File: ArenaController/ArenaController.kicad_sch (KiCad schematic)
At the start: 29 parts, among them J1 RJ45, J2 RJ45, J4 RJ45, J5 RJ45, J6 RJ45, J8 Screw_Terminal_01x04, J9 Barrel_Jack_MountingPin, Q1 FS3400, Q2 FS3400, Q3 FS3400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

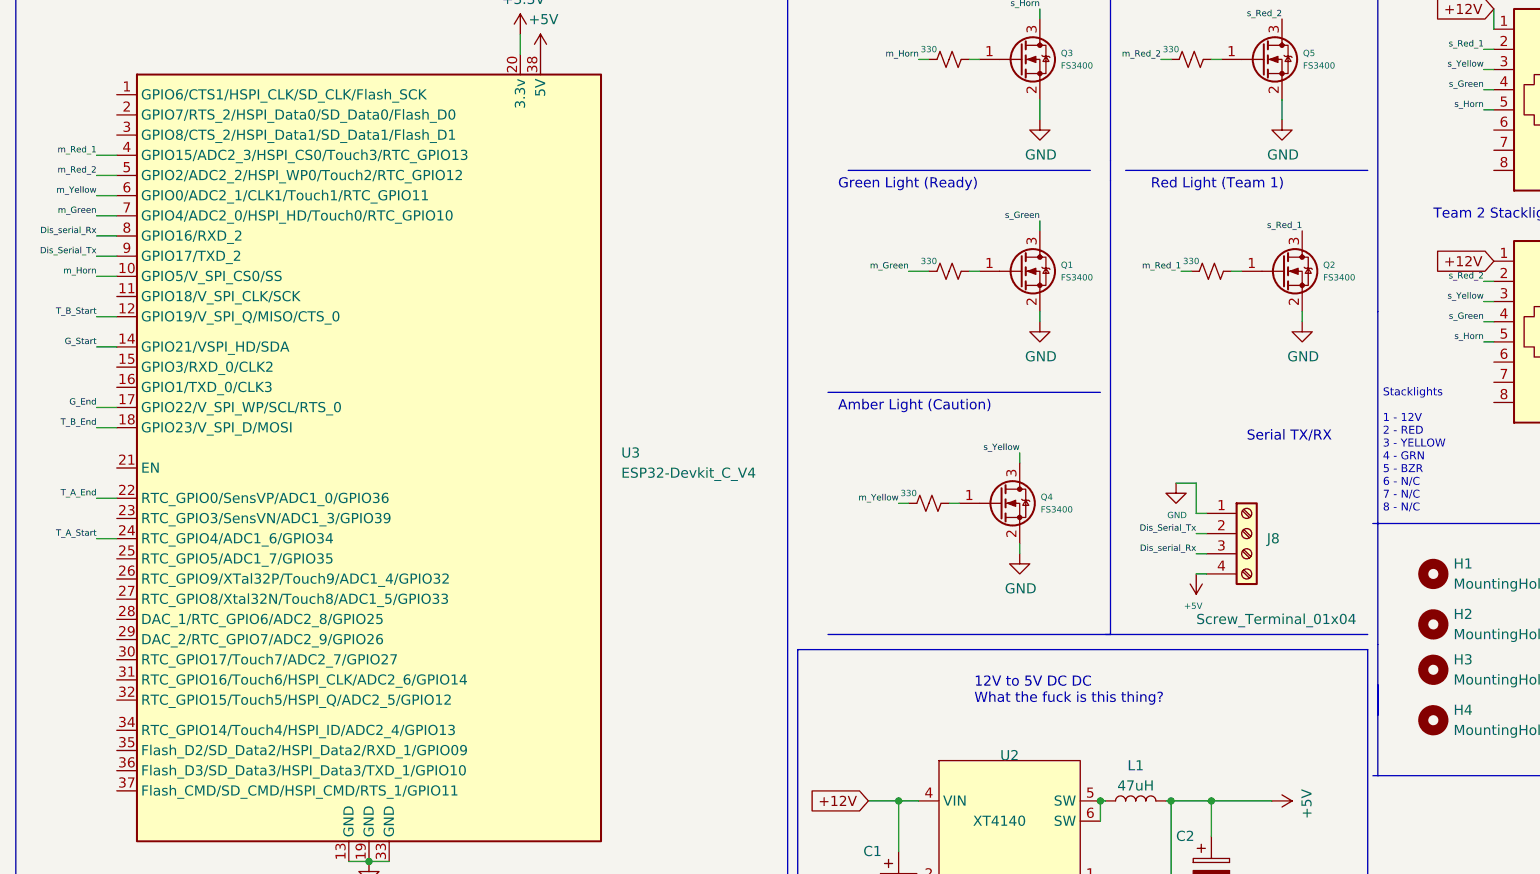
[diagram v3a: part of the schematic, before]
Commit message: Update PCB errors and also remove software from this repo.
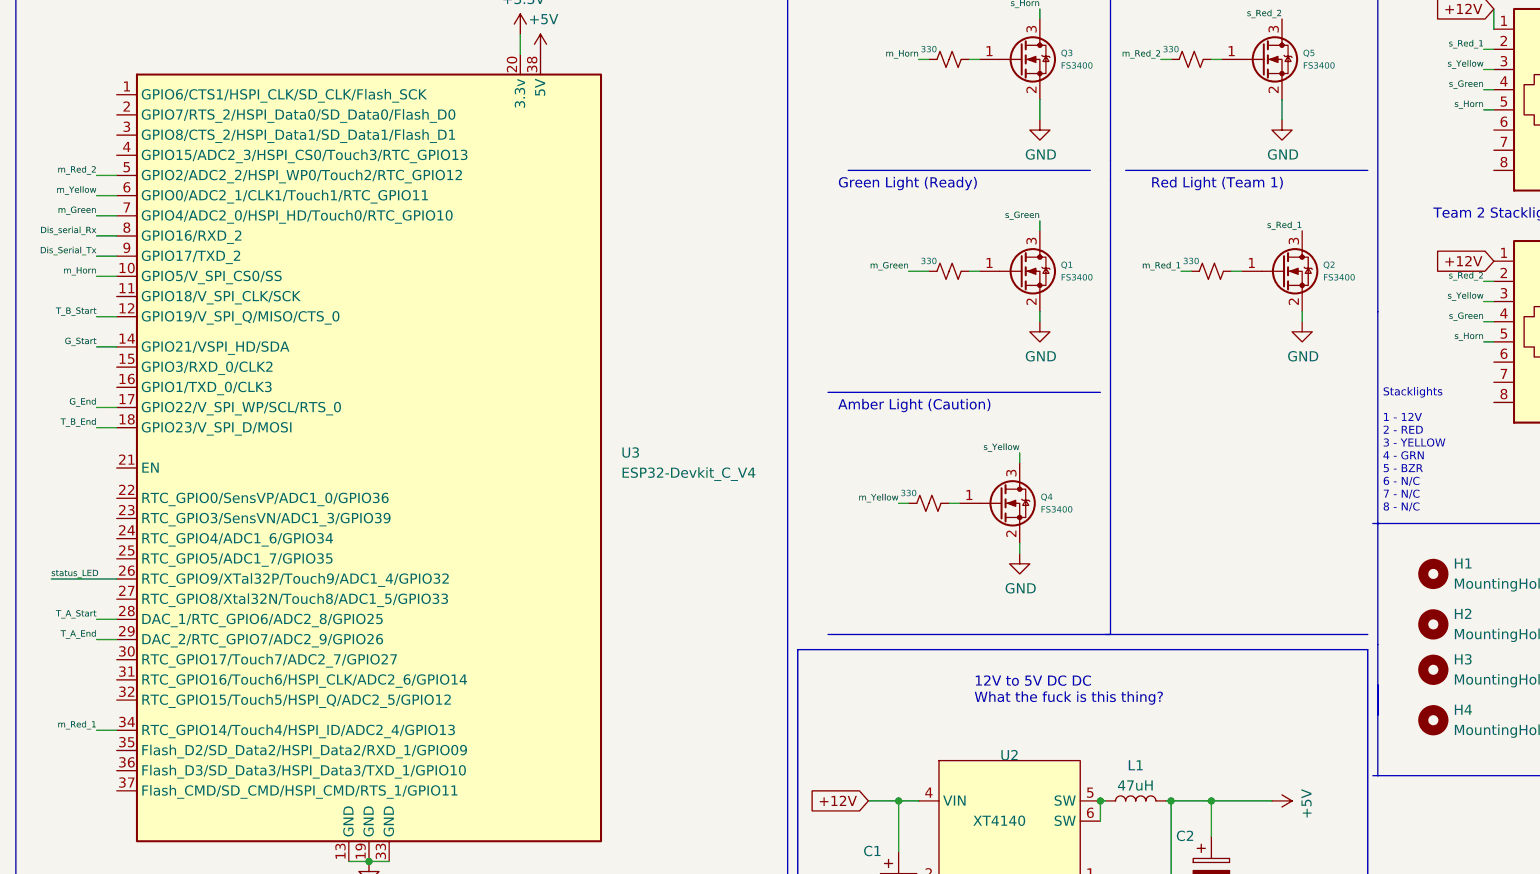
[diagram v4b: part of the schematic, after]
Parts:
- removed J8: Screw_Terminal_01x04, Connector_PinSocket_2.54mm:PinSocket_1x04_P2.54mm_Vertical, symbol Connector:Screw_Terminal_01x04
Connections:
- net T_A_End: now also U3.29 (DAC_2/RTC_GPIO7/ADC2_9/GPIO26); no longer U3.22 (RTC_GPIO0/SensVP/ADC1_0/GPIO36)
- net T_A_Start: now also U3.28 (DAC_1/RTC_GPIO6/ADC2_8/GPIO25); no longer U3.24 (RTC_GPIO4/ADC1_6/GPIO34)
- net m_Red_1: now also U3.34 (RTC_GPIO14/Touch4/HSPI_ID/ADC2_4/GPIO13); no longer U3.4 (GPIO15/ADC2_3/HSPI_CS0/Touch3/RTC_GPIO13)
- net status_LED: now also U3.26 (RTC_GPIO9/XTal32P/Touch9/ADC1_4/GPIO32)
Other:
- note removed: "Serial TX/RX"
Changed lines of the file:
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@@
   (title_block
     (title "Combat Arena Timing Control")
-    (date "2023-04-14")
-    (rev "0.4a")
+    (date "2023-04-29")
+    (rev "0.5")
     (company "Fair Use Building & Research Labs, 501c3")
     (comment 2 "Neil Flynn")
@@
     (stroke (width 0) (type default))
   )
-  (wire (pts (xy 165.735 92.71) (xy 164.465 92.71))
-    (stroke (width 0) (type default))
-  )
   (wire (pts (xy 243.84 63.5) (xy 248.92 63.5))
     (stroke (width 0) (type default))
@@
     (stroke (width 0) (type default))
   )
-  (wire (pts (xy 164.465 83.82) (xy 164.465 87.63))
-    (stroke (width 0) (type default))
-  )
-  (wire (pts (xy 165.735 90.17) (xy 164.465 90.17))
-    (stroke (width 0) (type default))
-  )
   (wire (pts (xy 137.16 30.48) (xy 135.89 30.48))
     (stroke (width 0) (type default))
@@
     (stroke (width 0) (type default))
   )
+  (wire (pts (xy 20.32 95.885) (xy 28.575 95.885))
+    (stroke (width 0) (type default))
+  )
   (polyline (pts (xy 187.325 120.65) (xy 187.325 104.14))
     (stroke (width 0) (type default))
@@
     (stroke (width 0) (type default))
   )
-  (wire (pts (xy 161.925 83.82) (xy 164.465 83.82))
-    (stroke (width 0) (type default))
-  )
   (polyline (pts (xy 227.33 15.24) (xy 227.33 67.31))
     (stroke (width 0) (type default))
@@
     (stroke (width 0) (type default))
   )
-  (wire (pts (xy 28.575 90.805) (xy 26.035 90.805))
+  (wire (pts (xy 28.575 100.965) (xy 26.035 100.965))
     (stroke (width 0) (type default))
   )
@@
     (stroke (width 0) (type default))
   )
-  (wire (pts (xy 165.735 95.25) (xy 164.465 95.25))
-    (stroke (width 0) (type default))
-  )
   (polyline (pts (xy 275.59 48.26) (xy 227.33 48.26))
     (stroke (width 0) (type default))
@@
     (stroke (width 0) (type default))
   )
-  (wire (pts (xy 165.735 87.63) (xy 164.465 87.63))
-    (stroke (width 0) (type default))
-  )
   (wire (pts (xy 57.785 131.445) (xy 60.325 131.445))
     (stroke (width 0) (type default))
@@
     (stroke (width 0) (type default))
   )
-  (wire (pts (xy 28.575 42.545) (xy 26.035 42.545))
+  (wire (pts (xy 28.575 114.935) (xy 26.035 114.935))
     (stroke (width 0) (type default))
   )
@@
     (stroke (width 0) (type default))
   )
-  (wire (pts (xy 28.575 85.725) (xy 26.035 85.725))
+  (wire (pts (xy 28.575 103.505) (xy 26.035 103.505))
     (stroke (width 0) (type default))
   )
@@
     (effects (font (size 1.27 1.27)) (justify left bottom))
   )
-  (text "Serial TX/RX\n" (at 170.815 78.74 0)
-    (effects (font (size 1.27 1.27)) (justify left bottom))
-  )
   (text "Team 1 Stacklight" (at 198.12 19.05 0)
     (effects (font (size 1.27 1.27)) (justify left bottom))
@@
     (effects (font (size 1 1)) (justify left bottom))
   )
-  (label "T_A_End" (at 26.035 85.725 180) (fields_autoplaced)
+  (label "T_A_End" (at 26.035 103.505 180) (fields_autoplaced)
     (effects (font (size 0.7874 0.7874)) (justify right bottom))
   )
@@
     (effects (font (size 0.7874 0.7874)) (justify right bottom))
   )
-  (label "Dis_serial_Rx" (at 164.465 92.71 180) (fields_autoplaced)
-    (effects (font (size 0.7874 0.7874)) (justify right bottom))
-  )
   (label "s_Green" (at 200.66 63.5 180) (fields_autoplaced)
     (effects (font (size 0.7874 0.7874)) (justify right bottom))
@@
     (effects (font (size 0.7874 0.7874)) (justify right bottom))
   )
-  (label "T_A_Start" (at 26.035 90.805 180) (fields_autoplaced)
+  (label "T_A_Start" (at 26.035 100.965 180) (fields_autoplaced)
     (effects (font (size 0.7874 0.7874)) (justify right bottom))
   )
@@
     (effects (font (size 0.7874 0.7874)) (justify right bottom))
   )
-  (label "m_Red_1" (at 26.035 42.545 180) (fields_autoplaced)
+  (label "m_Red_1" (at 26.035 114.935 180) (fields_autoplaced)
     (effects (font (size 0.7874 0.7874)) (justify right bottom))
   )
@@
     (effects (font (size 0.7874 0.7874)) (justify right bottom))
   )
-  (label "Dis_Serial_Tx" (at 164.465 90.17 180) (fields_autoplaced)
-    (effects (font (size 0.7874 0.7874)) (justify right bottom))
+  (label "status_LED" (at 20.32 95.885 0) (fields_autoplaced)
+    (effects (font (size 0.7874 0.7874)) (justify left bottom))
   )
   (label "m_Red_2" (at 160.02 30.48 180) (fields_autoplaced)
@@
     )
   )
-  (symbol (lib_id "power:+5V") (at 164.465 95.25 180) (unit 1)
-    (in_bom yes) (on_board yes) (dnp no)
-    (property "Reference" "#PWR0125" (at 164.465 91.44 0)
-      (effects (font (size 0.7874 0.7874)) hide)
-    )
-    (property "Value" "+5V" (at 164.084 99.2886 0)
-      (effects (font (size 0.7874 0.7874)))
-    )
-    (property "Footprint" "" (at 164.465 95.25 0)
-      (effects (font (size 1.27 1.27)) hide)
-    )
-    (property "Datasheet" "" (at 164.465 95.25 0)
-      (effects (font (size 1.27 1.27)) hide)
-    )
-    (pin "1")
-    (instances
-      (project "ArenaController"
-        (path "/156576da-4c7a-4c71-af43-7540e3a24bd3"
-          (reference "#PWR0125") (unit 1)
-        )
-      )
-    )
-  )
   (symbol (lib_id "symbols:FS3400") (at 175.26 57.15 0) (unit 1)
     (in_bom yes) (on_board yes) (dnp no)
@@
         (path "/156576da-4c7a-4c71-af43-7540e3a24bd3"
           (reference "Q2") (unit 1)
-        )
-      )
-    )
-  )
-  (symbol (lib_id "power:GND") (at 161.925 83.82 0) (unit 1)
-    (in_bom yes) (on_board yes) (dnp no)
-    (property "Reference" "#PWR0126" (at 161.925 90.17 0)
-      (effects (font (size 1.27 1.27)) hide)
-    )
-    (property "Value" "GND" (at 162.052 87.8586 0)
-      (effects (font (size 0.7874 0.7874)))
-    )
-    (property "Footprint" "" (at 161.925 83.82 0)
-      (effects (font (size 1.27 1.27)) hide)
-    )
-    (property "Datasheet" "" (at 161.925 83.82 0)
-      (effects (font (size 1.27 1.27)) hide)
-    )
-    (pin "1")
-    (instances
-      (project "ArenaController"
-        (path "/156576da-4c7a-4c71-af43-7540e3a24bd3"
-          (reference "#PWR0126") (unit 1)
         )
       )
@@
         )
       )
-    )
-  )
-  (symbol (lib_id "Connector:Screw_Terminal_01x04") (at 170.815 90.17 0) (unit 1)
-    (in_bom yes) (on_board yes) (dnp no)
-    (property "Reference" "J8" (at 173.355 90.805 0)
-      (effects (font (size 1.27 1.27)) (justify left))
-    )
-    (property "Value" "Screw_Terminal_01x04" (at 164.465 100.965 0)
-      (effects (font (size 1.27 1.27)) (justify left))
-    )
-    (property "Footprint" "Connector_PinSocket_2.54mm:PinSocket_1x04_P2.54mm_Vertical" (at 170.815 90.17 0)
-      (effects (font (size 1.27 1.27)) hide)
-    )
-    (property "Datasheet" "~" (at 170.815 90.17 0)
-      (effects (font (size 1.27 1.27)) hide)
-    )
-    (pin "1")
-    (pin "2")
-    (pin "3")
-    (pin "4")
-    (instances
-      (project "ArenaController"
-        (path "/156576da-4c7a-4c71-af43-7540e3a24bd3"
-          (reference "J8") (unit 1)
-        )
-      )

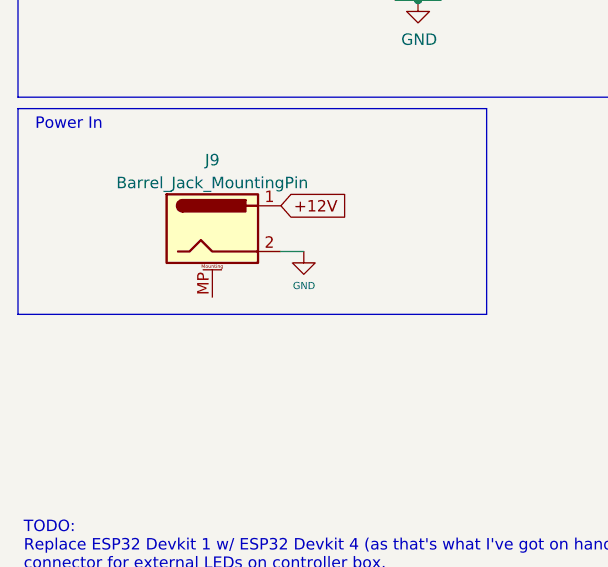
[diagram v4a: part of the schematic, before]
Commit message: Swap to a footprint with the correctly named pin in our project repo.  Yay!
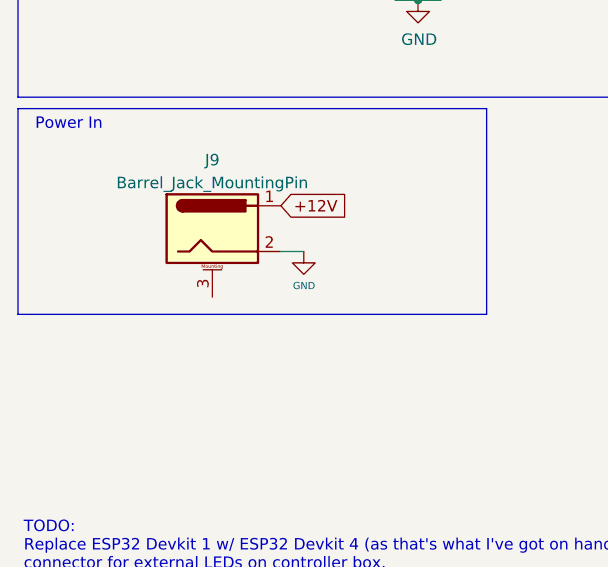
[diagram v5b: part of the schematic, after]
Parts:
- J9: symbol Connector:Barrel_Jack_MountingPin -> symbols:Barrel_Jack_MountingPin
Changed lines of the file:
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@@
     )
   )
-  (symbol (lib_id "Connector:Barrel_Jack_MountingPin") (at 37.465 156.845 0) (unit 1)
+  (symbol (lib_id "symbols:Barrel_Jack_MountingPin") (at 37.465 156.845 0) (unit 1)
     (in_bom yes) (on_board yes) (dnp no) (fields_autoplaced)
     (property "Reference" "J9" (at 37.465 149.225 0)
@@
     (pin "1")
     (pin "2")
-    (pin "MP")
+    (pin "3")
     (instances
       (project "ArenaController"

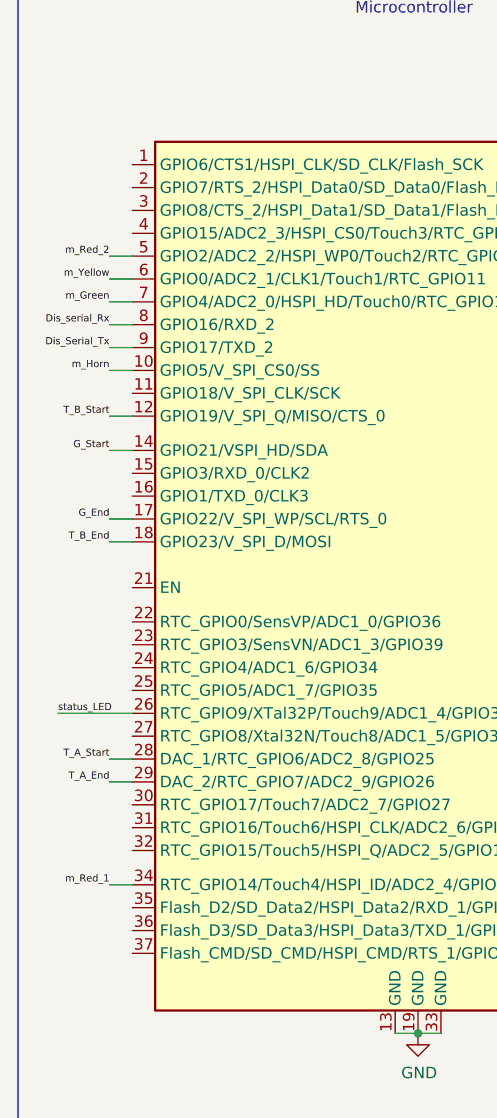
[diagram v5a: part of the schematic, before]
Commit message: Added initial teamsign and update symbol mistakes, mostly.
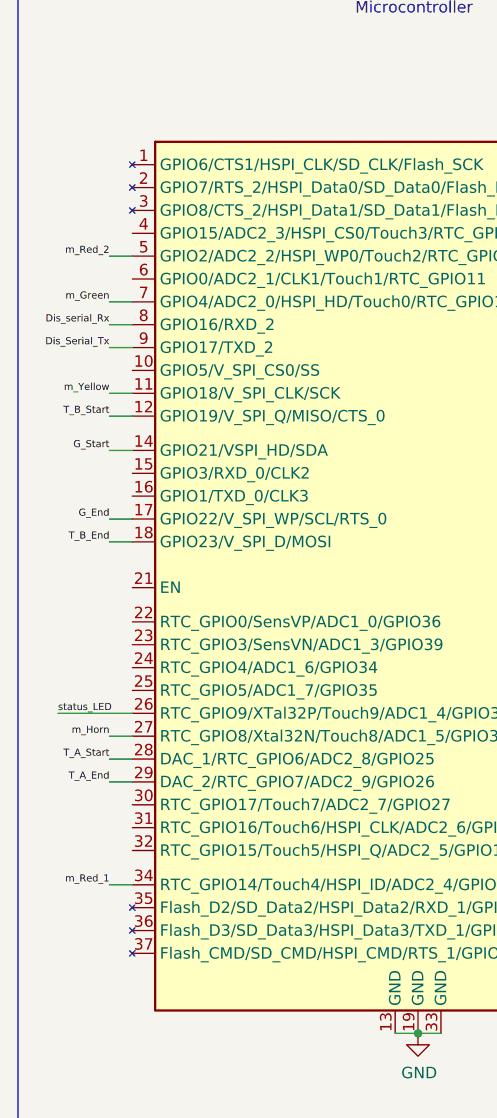
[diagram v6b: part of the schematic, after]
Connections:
- net m_Horn: now also U3.27 (RTC_GPIO8/Xtal32N/Touch8/ADC1_5/GPIO33); no longer U3.10 (GPIO5/V_SPI_CS0/SS)
- net m_Yellow: now also U3.11 (GPIO18/V_SPI_CLK/SCK); no longer U3.6 (GPIO0/ADC2_1/CLK1/Touch1/RTC_GPIO11)
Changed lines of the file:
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@@
     (stroke (width 0) (type default))
   )
-  (wire (pts (xy 28.575 57.785) (xy 26.035 57.785))
+  (wire (pts (xy 28.575 98.425) (xy 26.035 98.425))
     (stroke (width 0) (type default))
   )
@@
     (stroke (width 0) (type default))
   )
-  (wire (pts (xy 28.575 47.625) (xy 26.035 47.625))
+  (wire (pts (xy 28.575 60.325) (xy 26.035 60.325))
     (stroke (width 0) (type default))
   )
@@
     (effects (font (size 0.7874 0.7874)) (justify right bottom))
   )
-  (label "m_Horn" (at 26.035 57.785 180) (fields_autoplaced)
+  (label "m_Horn" (at 26.035 98.425 180) (fields_autoplaced)
     (effects (font (size 0.7874 0.7874)) (justify right bottom))
   )
@@
     (effects (font (size 0.7874 0.7874)) (justify right bottom))
   )
-  (label "m_Yellow" (at 26.035 47.625 180) (fields_autoplaced)
-    (effects (font (size 0.7874 0.7874)) (justify right bottom))
-  )
+  (label "m_Yellow" (at 26.035 60.325 180) (fields_autoplaced)
+    (effects (font (size 0.7874 0.7874)) (justify right bottom))
+  )

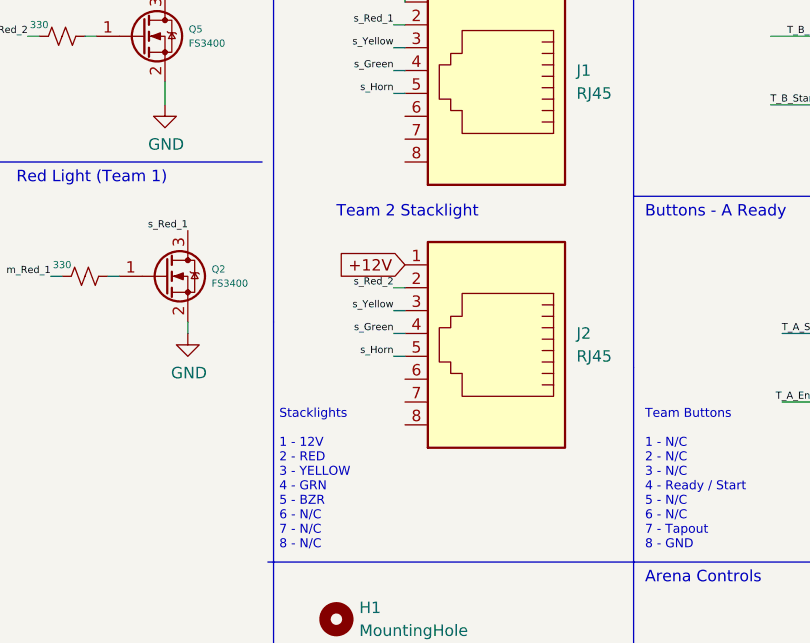
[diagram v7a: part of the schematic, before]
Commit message: Add SK6812-Side-A footprint/symbol to working area, as well as swapped to a stacklight connection that has a ground pin at the end for generic 12v power use.  yay!
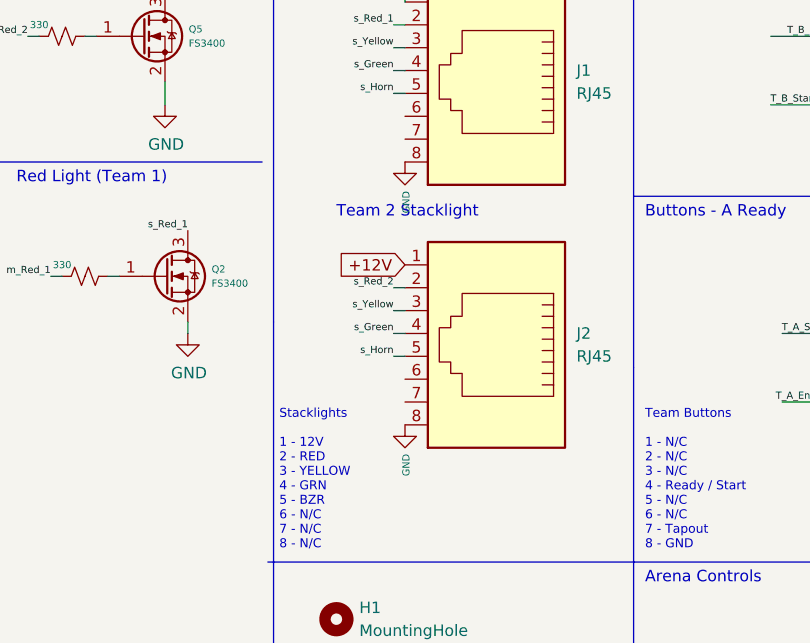
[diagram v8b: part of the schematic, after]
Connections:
- net GND: now also J1.8, J2.8
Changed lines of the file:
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@@
+    )
+  )
+  (symbol (lib_id "power:GND") (at 201.93 44.45 0) (unit 1)
+    (in_bom yes) (on_board yes) (dnp no)
+    (property "Reference" "#PWR09" (at 201.93 50.8 0)
+      (effects (font (size 0.7874 0.7874)) hide)
+    )
+    (property "Value" "GND" (at 202.057 47.6758 90)
+      (effects (font (size 0.7874 0.7874)) (justify right))
+    )
+    (property "Footprint" "" (at 201.93 44.45 0)
+      (effects (font (size 1.27 1.27)) hide)
+    )
+    (property "Datasheet" "" (at 201.93 44.45 0)
+      (effects (font (size 1.27 1.27)) hide)
+    )
+    (pin "1")
+    (instances
+      (project "ArenaController"
+        (path "/156576da-4c7a-4c71-af43-7540e3a24bd3"
+          (reference "#PWR09") (unit 1)
+        )
+      )
     )
   )
@@
         )
       )
+    )
+  )
+  (symbol (lib_id "power:GND") (at 201.93 73.66 0) (unit 1)
+    (in_bom yes) (on_board yes) (dnp no)
+    (property "Reference" "#PWR08" (at 201.93 80.01 0)
+      (effects (font (size 0.7874 0.7874)) hide)
+    )
+    (property "Value" "GND" (at 202.057 76.8858 90)
+      (effects (font (size 0.7874 0.7874)) (justify right))
+    )
+    (property "Footprint" "" (at 201.93 73.66 0)
+      (effects (font (size 1.27 1.27)) hide)
+    )
+    (property "Datasheet" "" (at 201.93 73.66 0)
+      (effects (font (size 1.27 1.27)) hide)
+    )
+    (pin "1")
+    (instances
+      (project "ArenaController"
+        (path "/156576da-4c7a-4c71-af43-7540e3a24bd3"
+          (reference "#PWR08") (unit 1)
+        )
+      )
